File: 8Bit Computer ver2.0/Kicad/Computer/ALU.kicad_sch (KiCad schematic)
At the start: 0 parts

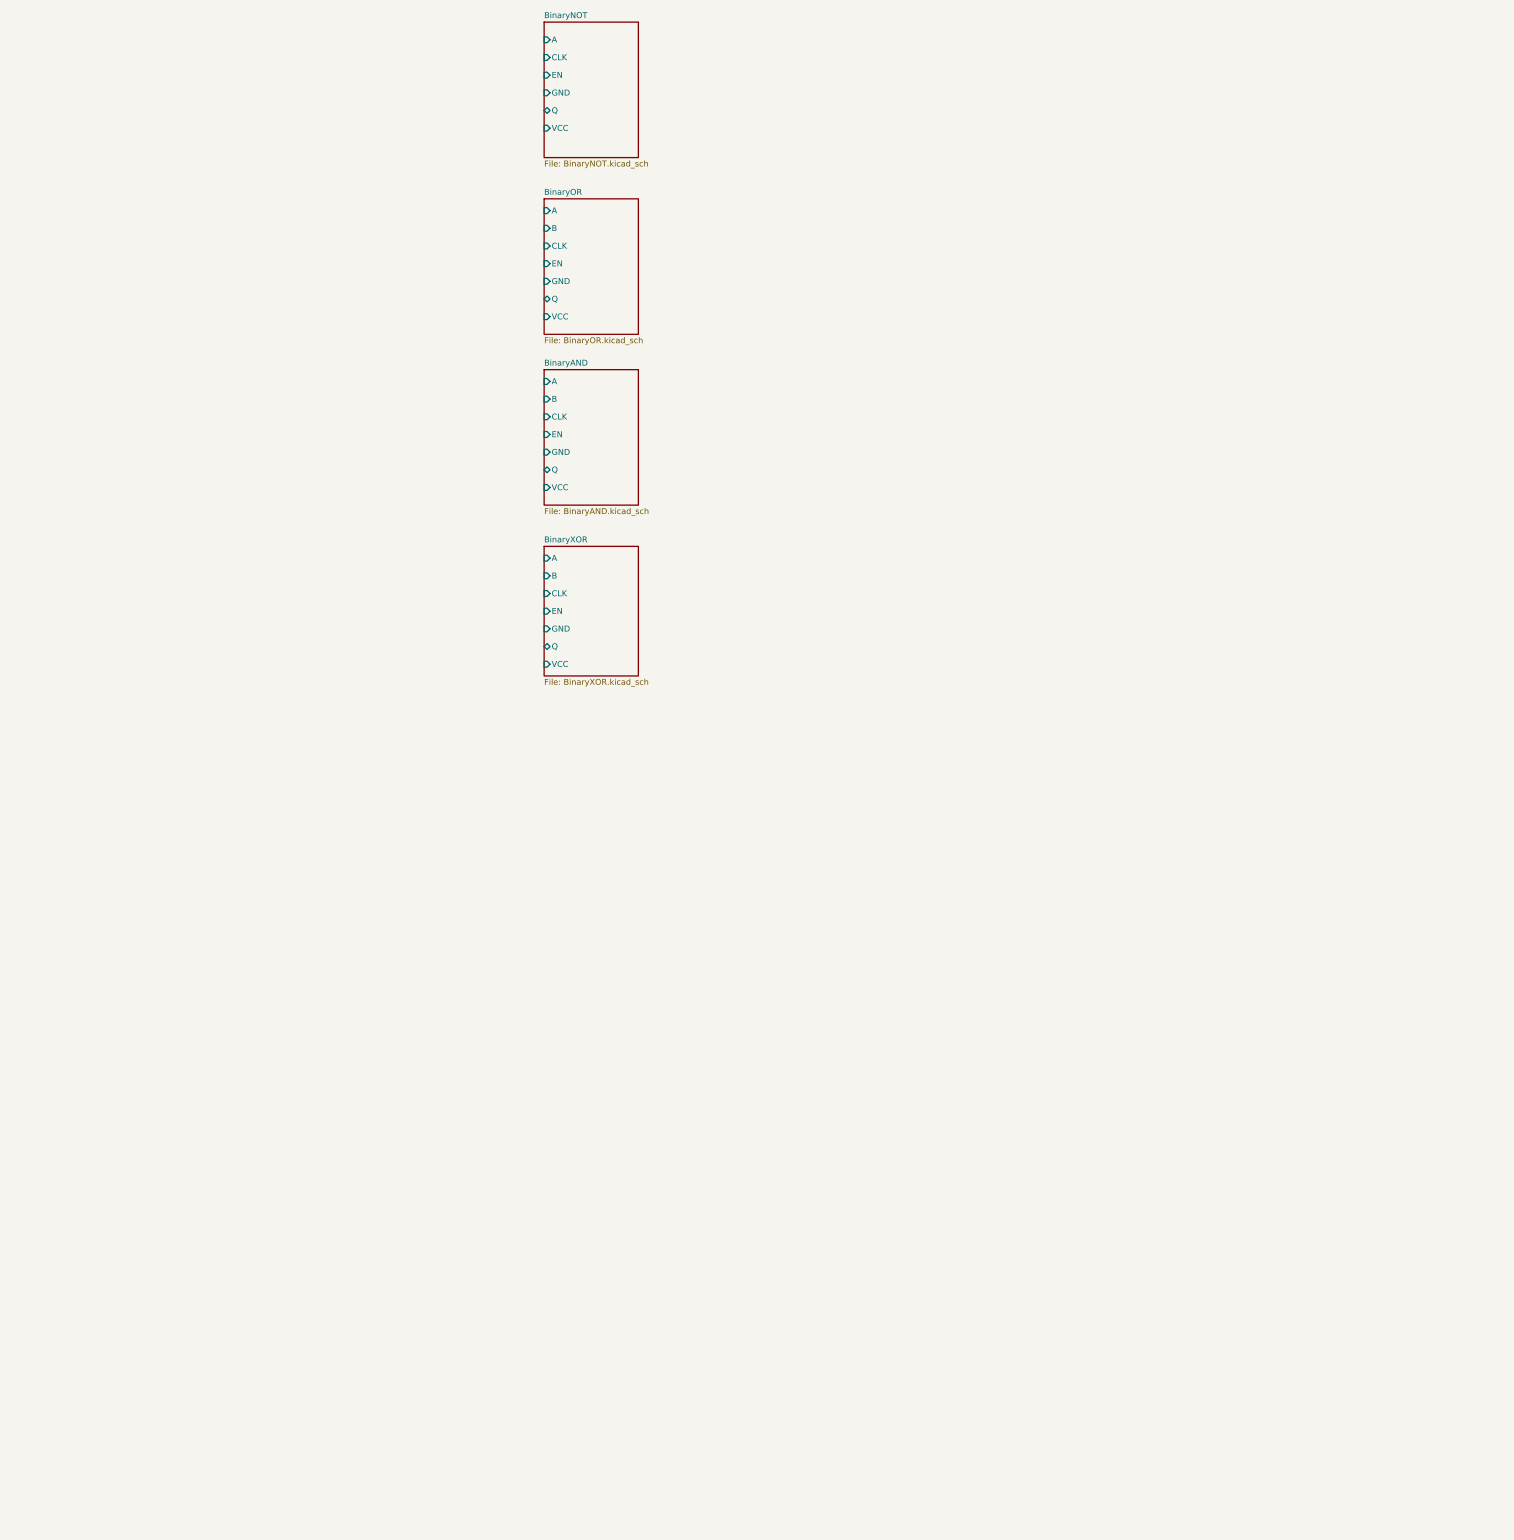
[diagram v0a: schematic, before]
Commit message: parts,Kicad
added 74HCS574 to Kicad
Kicad:
ALU->added Bitwise NOT,OR,XOR,AND
ALU->added A,B 8in OR
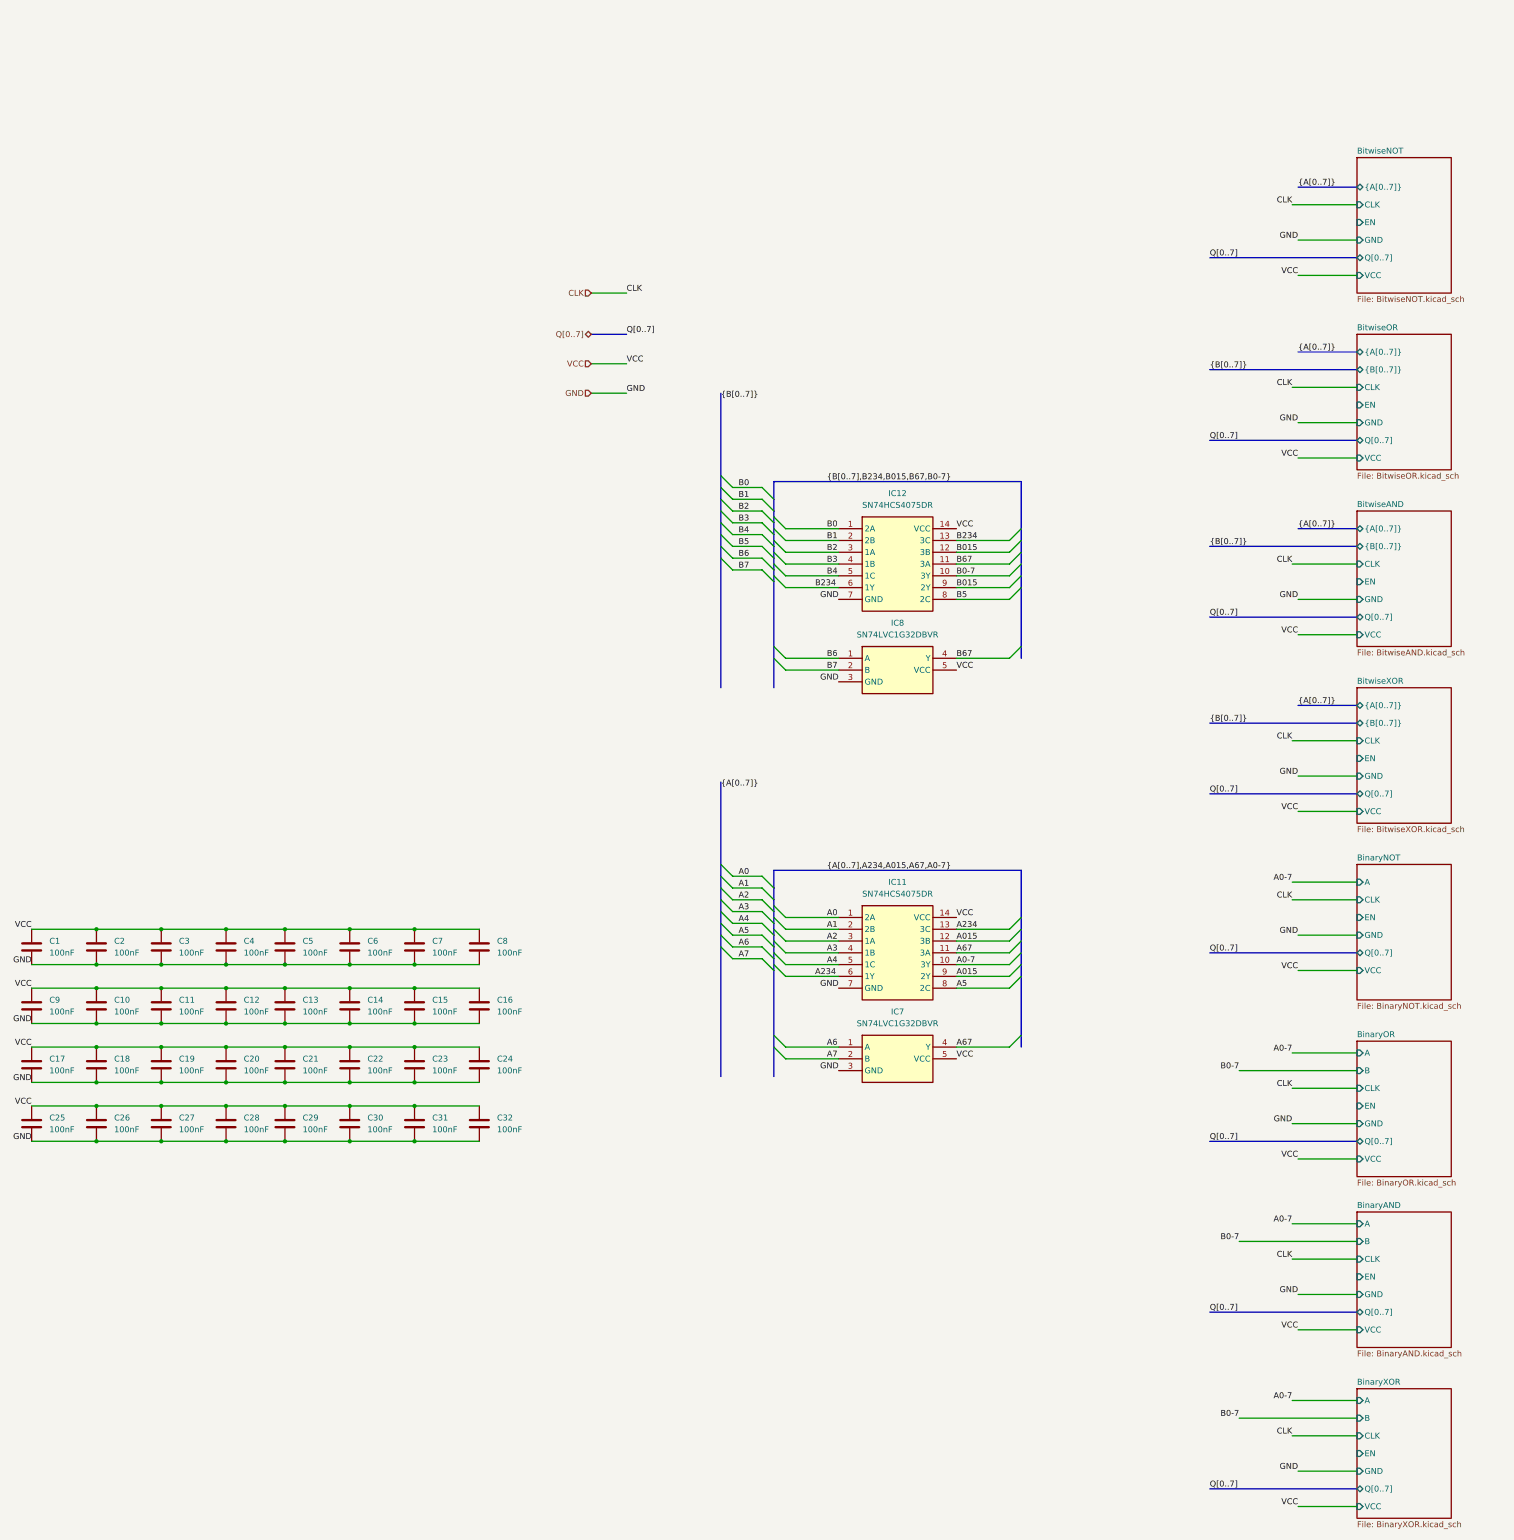
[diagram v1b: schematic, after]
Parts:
- added C1, C10, C11, C12, C13, C14, C15, C16, C17, C18, C19, C2, C20, C21, C22, C23, C24, C25, C26, C27, C28, C29, C3, C30, C31, C32, C4, C5, C6, C7, C8, C9: 100nF, Capacitor_SMD:C_1206_3216Metric_Pad1.33x1.80mm_HandSolder, symbol Device:C
- added IC11, IC12: SN74HCS4075DR, Samacsys:SOIC127P600X175-14N, symbol Samacsys:SN74HCS4075DR
- added IC7, IC8: SN74LVC1G32DBVR, Samacsys:SOT95P280X145-5N, symbol Samacsys:SN74LVC1G32DBVR
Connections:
- new net A0: IC11.1 (2A)
- new net A0-7: IC11.10 (3Y)
- new net A015: IC11.12 (3B), IC11.9 (2Y)
- new net A1: IC11.2 (2B)
- new net A2: IC11.3 (1A)
- new net A234: IC11.13 (3C), IC11.6 (1Y)
- new net A3: IC11.4 (1B)
- new net A4: IC11.5 (1C)
- new net A5: IC11.8 (2C)
- new net A6: IC7.1 (A)
- new net A67: IC11.11 (3A), IC7.4 (Y)
- new net A7: IC7.2 (B)
- new net B0: IC12.1 (2A)
- new net B0-7: IC12.10 (3Y)
- new net B015: IC12.12 (3B), IC12.9 (2Y)
- new net B1: IC12.2 (2B)
- new net B2: IC12.3 (1A)
- new net B234: IC12.13 (3C), IC12.6 (1Y)
- new net B3: IC12.4 (1B)
- new net B4: IC12.5 (1C)
- new net B5: IC12.8 (2C)
- new net B6: IC8.1 (A)
- new net B67: IC12.11 (3A), IC8.4 (Y)
- new net B7: IC8.2 (B)
- new net GND: C1.1, C10.1, C11.1, C12.1, C13.1, C14.1, C15.1, C16.1, C17.1, C18.1, C19.1, C2.1, C20.1, C21.1, C22.1, C23.1, C24.1, C25.1, C26.1, C27.1, C28.1, C29.1, C3.1, C30.1, C31.1, C32.1, C4.1, C5.1, C6.1, C7.1, C8.1, C9.1, IC11.7 (GND), IC12.7 (GND), IC7.3 (GND), IC8.3 (GND)
- new net VCC: C1.2, C10.2, C11.2, C12.2, C13.2, C14.2, C15.2, C16.2, C17.2, C18.2, C19.2, C2.2, C20.2, C21.2, C22.2, C23.2, C24.2, C25.2, C26.2, C27.2, C28.2, C29.2, C3.2, C30.2, C31.2, C32.2, C4.2, C5.2, C6.2, C7.2, C8.2, C9.2, IC11.14 (VCC), IC12.14 (VCC), IC7.5 (VCC), IC8.5 (VCC)
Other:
- added sheet BitwiseAND (BitwiseAND.kicad_sch)
- added sheet BitwiseNOT (BitwiseNOT.kicad_sch)
- added sheet BitwiseOR (BitwiseOR.kicad_sch)
- added sheet BitwiseXOR (BitwiseXOR.kicad_sch)
- sheet BinaryAND ports: added Q[0..7]; removed Q
- sheet BinaryNOT ports: added Q[0..7]; removed Q
- sheet BinaryOR ports: added Q[0..7]; removed Q
- sheet BinaryXOR ports: added Q[0..7]; removed Q

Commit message: Kicad,parts
Kicad:
added FlagRegister
began Inc, Comp
parts:
added comparator for P>Q 682
added faster sram 12ns AS7C
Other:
- added sheet Comparator (Comparator.kicad_sch)
- added sheet FlagRegister (FlagRegister.kicad_sch)
- added sheet Incrementor (Incrementor.kicad_sch)
- sheet BinaryAND ports: added ~{CLK}; removed CLK
- sheet BinaryNOT ports: added ~{CLK}; removed CLK
- sheet BinaryOR ports: added ~{CLK}; removed CLK
- sheet BinaryXOR ports: added ~{CLK}; removed CLK
- sheet BitwiseAND ports: added ~{CLK}; removed CLK
- sheet BitwiseNOT ports: added ~{CLK}; removed CLK
- sheet BitwiseOR ports: added ~{CLK}; removed CLK
- sheet BitwiseXOR ports: added ~{CLK}; removed CLK
- moved on the sheet: C1, C10, C11, C12, C13, C14, C15, C16, C17, C18, C19, C2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

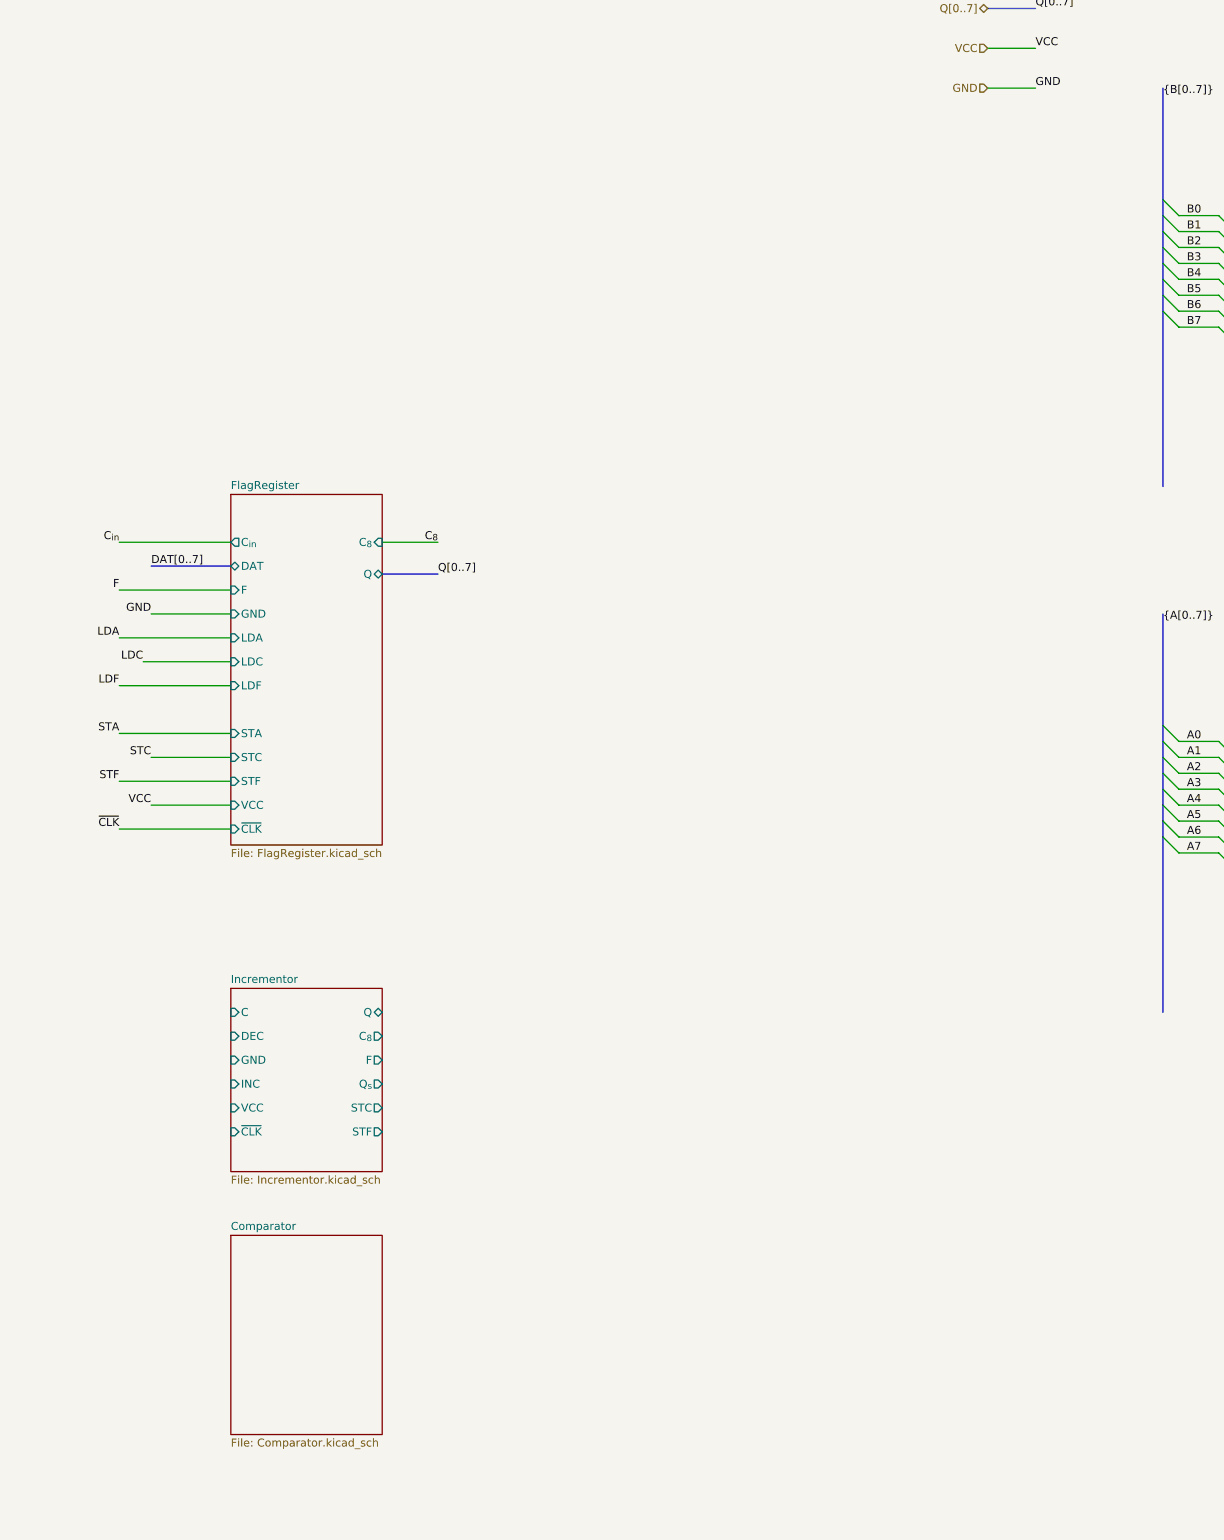
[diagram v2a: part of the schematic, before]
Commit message: parts,Kicad
parts:
changed 8xDlatch HCS to ABT 574
waiting for SRAM CAD Model
Kicad:
imported AHC types of ICs
added ProgrammeCounter
finished Comparator
changed all HCS to AHC except 3in OR ->no AHC Version
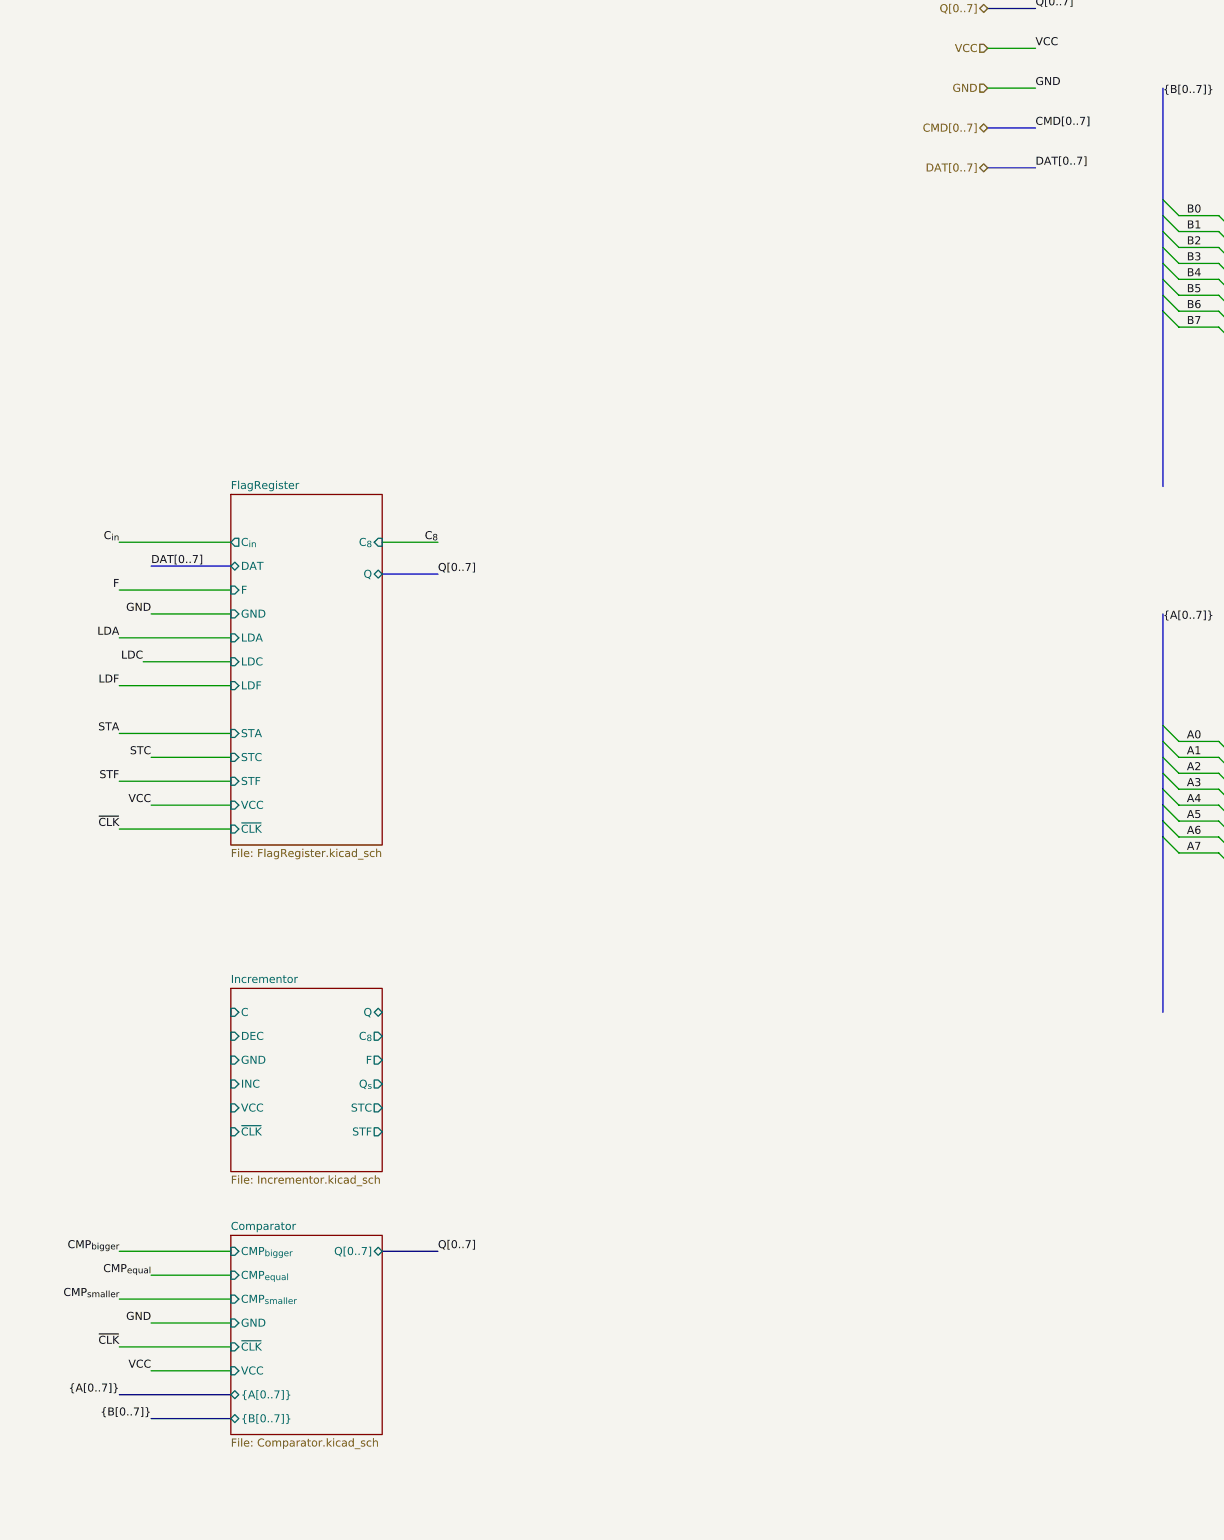
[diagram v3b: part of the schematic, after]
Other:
- sheet Comparator ports: added CMP_{bigger}, CMP_{equal}, CMP_{smaller}, GND, Q[0..7], VCC, {A[0..7]}, {B[0..7]}, ~{CLK}; removed none
